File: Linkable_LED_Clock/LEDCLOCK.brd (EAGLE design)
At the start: 41.4 x 26.7 mm, 10 parts, among them Q1 MMBT2907ALT1SMD, Q2 MMBT2907ALT1SMD, Q3 MMBT2907ALT1SMD, Q4 MMBT2907ALT1SMD, Q5 MMBT2907ALT1SMD

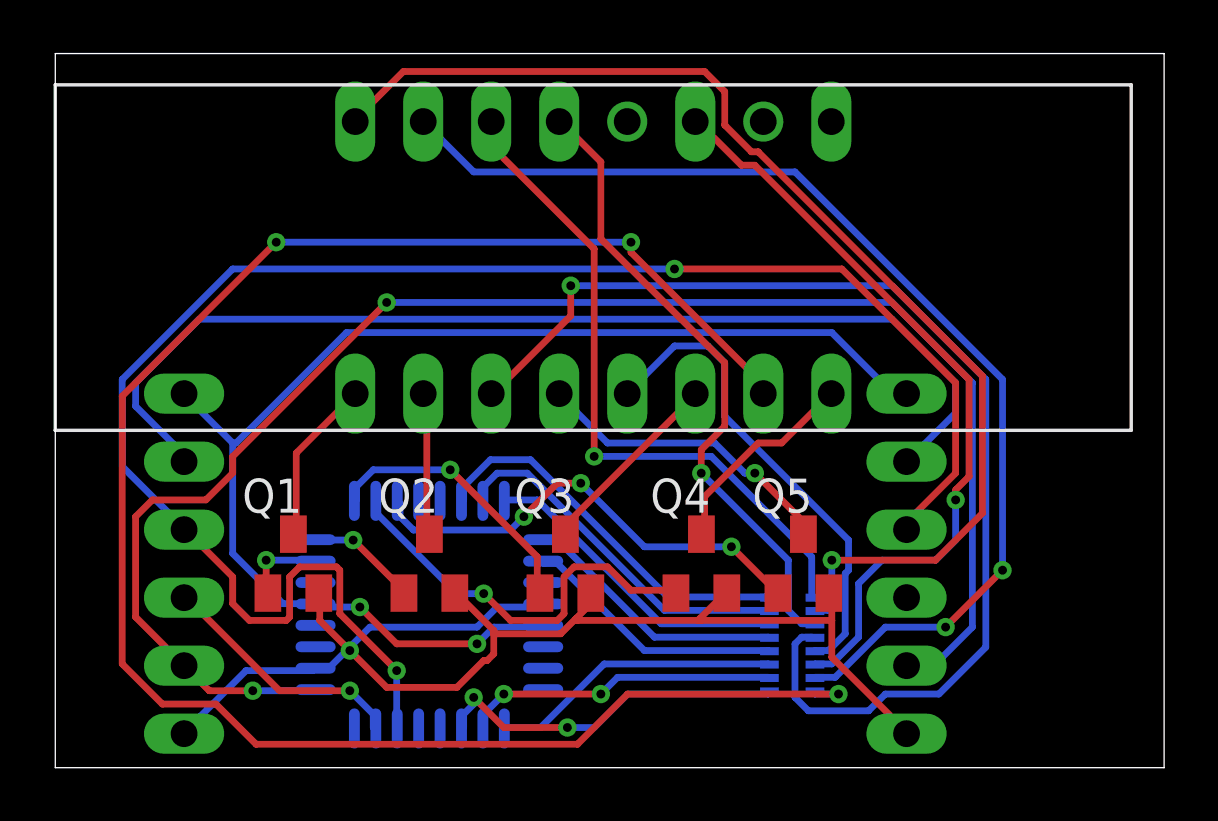
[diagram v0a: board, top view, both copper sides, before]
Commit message: Board now flush
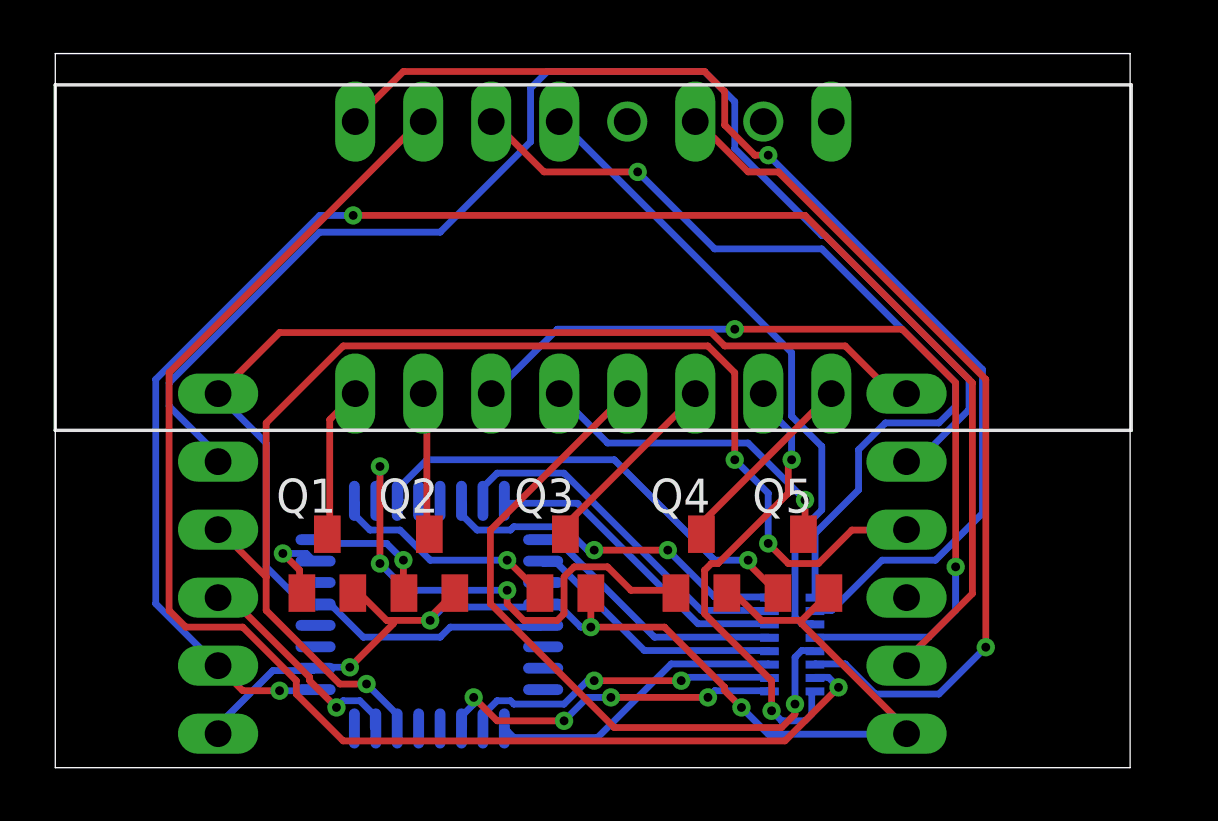
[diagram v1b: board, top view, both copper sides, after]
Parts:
- moved U$2 1.27 mm to (6.08, 7.62)
- moved Q1 1.27 mm to (10.2, 7.62)
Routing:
- net RDP: track 68.8 -> 17.5 mm, vias 3 -> 2
- net SS: track 63.7 -> 48.5 mm, vias 2 -> 3
- net RD: track 43.4 -> 33.4 mm, vias 1 -> 2
- net RG: track 41.4 -> 51.4 mm, vias 2 -> 1
- net RESET: track 40.0 -> 49.6 mm
- net RE: track 18.1 -> 26.4 mm, vias 0 -> 1
- net RA: track 25.4 -> 32.8 mm
- net VCC: track 49.5 -> 45.3 mm, vias 1 -> 4
- net DIGIT4: track 15.4 -> 19.3 mm, vias 1 -> 3
- net RF: track 28.8 -> 32.4 mm
- net CLK: track 60.0 -> 62.9 mm
- net DIGIT3: track 10.3 -> 8.65 mm
- net GND: track 47.8 -> 46.4 mm, vias 2 -> 0
- net A: track 14.6 -> 13.4 mm, vias 0 -> 2
- net MOSI: track 9.48 -> 8.50 mm
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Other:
- board size 41.4 x 26.7 mm -> 40.1 x 26.7 mm
